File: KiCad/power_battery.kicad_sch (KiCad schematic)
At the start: 52 parts, among them IC1 BQ26221PW, J2 Conn_01x03_BATT, Q1 AO3400A, Q2 AO3400A, U2 DW01A, U3 TXS0101DBV, U4 BQ51050BRHL, U5 PAM2306AYPKE

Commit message: First Draft PCB Layout
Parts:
- renumbered C11 to C12, C12 to C13, C13 to C14, C14 to C15, C15 to C16, C16 to C17, C17 to C18, C18 to C19, C19 to C20, C20 to C21, C21 to C22, C22 to C23, C23 to C24, C24 to C25, C25 to C26, C26 to C27, C27 to C28, C28 to C29, C29 to C30, C30 to C31, C31 to C32, C32 to C33, C33 to C34
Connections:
- net AC1_C: now reaches C22.1, L1.2
- net /Red_LED_R: now reaches D2.2 (A), R16.1
- net /Blue_LED_R: now reaches D3.2 (A), R17.1
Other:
- moved on the sheet: D2, D3, R16, R17

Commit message: Implement Comments, Working on PCB Layout
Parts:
- removed C15, C16, C17: 100n, Capacitor_SMD:C_0402_1005Metric, symbol Device:C
- removed IC1: BQ26221PW, TI-BQ26221PW:SOP65P640X120-8N, symbol BQ26221PW:BQ26221PW
- removed R10, R9: 100k, Resistor_SMD:R_0402_1005Metric, symbol Device:R
- removed R11: 20m, Resistor_SMD:R_0402_1005Metric, symbol Device:R
- removed R4, R6, R8: 10k, Resistor_SMD:R_0402_1005Metric, symbol Device:R
- removed U3: TXS0101DBV, Package_TO_SOT_SMD:SOT-23-6, symbol Logic_LevelTranslator:TXS0101DBV
- added U3: MAX17262REWL_T, MAX17262REWL_T:BGA9N40P3X3_144X146X69N, symbol MAX17262REWL_T:MAX17262REWL_T
- renumbered C18 to C15, C19 to C16, C20 to C17, C21 to C18, C22 to C19, C23 to C20, C24 to C21, C25 to C22, C26 to C23, C27 to C24, C28 to C25, C29 to C26, C30 to C27, C31 to C28, C32 to C29, C33 to C30, C34 to C31, R16 to R10, R17 to R11, R7 to R4, R12 to R6, R13 to R7, R14 to R8, R15 to R9
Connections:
- net BAT_STAT_SRP is gone; now on net BATT+: C13.1
- net +1V8: no longer R5.1
- net BATT-: no longer C13.2, C14.2
- net GND: now also C13.2, C14.2, U3.B2 (ALRT), U3.C3 (GND)
- net TS_CTRL: now also R5.1
- net BATTERY_PWR renamed BATT+
- net BATT+: now also U3.A2 (BATT); no longer C28.1, C29.1, U5.1 (VIN2), U5.12 (EN2), U5.6 (EN1), U5.7 (VIN1)
- net BATT_STATUS_HDQ renamed TS_CTRL_R
- net TS_CTRL_R: now also U3.A1 (TH)
- net BAT_STAT_SRN renamed Stat_REG
- net Stat_REG: now also U3.C2 (REG)
- new net Batt_Status_SCL: U3.B1 (SCL)
- new net Batt_Status_SDA: U3.C1 (SDA)
- new net SYS_PWR: C28.1, C29.1, U3.B3 (SYS), U5.1 (VIN2), U5.12 (EN2), U5.6 (EN1), U5.7 (VIN1)
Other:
- note added: "TH - BATT if no Thermistor"
- note added: "TODO: Check Saturation Current @ 2u2"
- note removed: "GPIO unused for now"

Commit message: PCB Layout V0.1 with errors
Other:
- company: ETH Zurich: Center for Project Based Learning -> ETH Zürich: Center for Project Based Learning
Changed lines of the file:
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@@
 		(date "2026-03-09")
 		(rev "0.0.2")
-		(company "ETH Zurich: Center for Project Based Learning")
+		(company "ETH Zürich: Center for Project Based Learning")
 	)
 	(rectangle

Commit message: Fix Schematic Symbol Footprint Filter from Library for Battery
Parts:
- J2: footprint Connector_JST:JST_PH_S3B-PH-K_1x03_P2.00mm_Horizontal -> Connector_JST:JST_PH_S3B-PH-SM4-TB_1x03-1MP_P2.00mm_Horizontal
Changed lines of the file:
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@@
 			)
 		)
-		(property "Footprint" "Connector_JST:JST_PH_S3B-PH-K_1x03_P2.00mm_Horizontal"
+		(property "Footprint" "Connector_JST:JST_PH_S3B-PH-SM4-TB_1x03-1MP_P2.00mm_Horizontal"
 			(at 21.59 49.53 0)
 			(effects

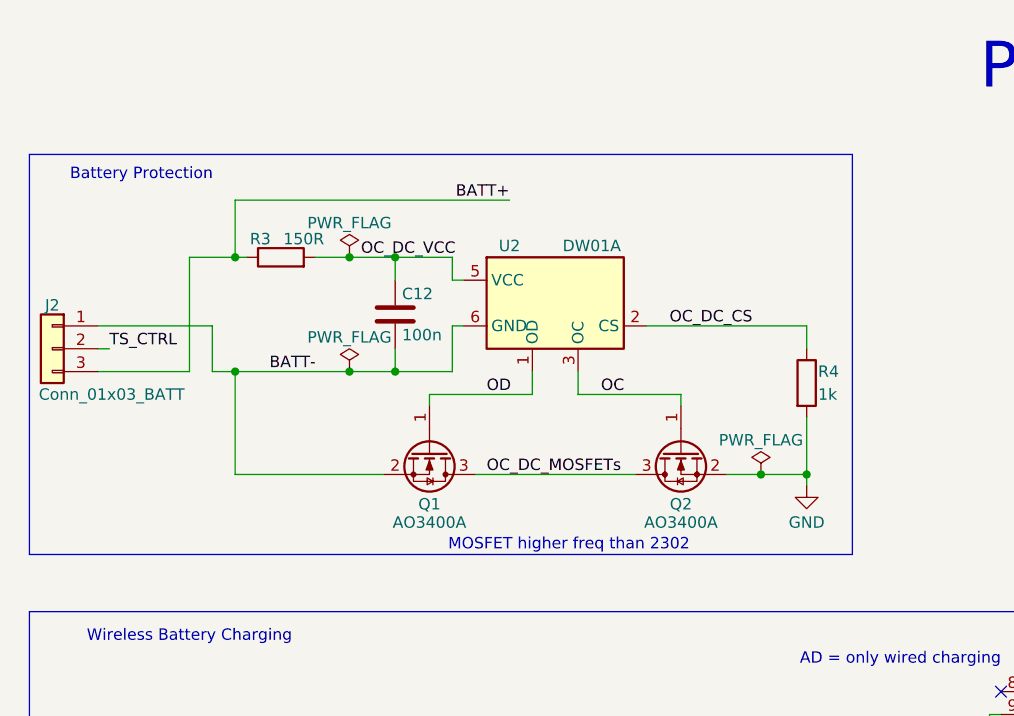
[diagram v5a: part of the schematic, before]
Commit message: Use SMT connector for Battery
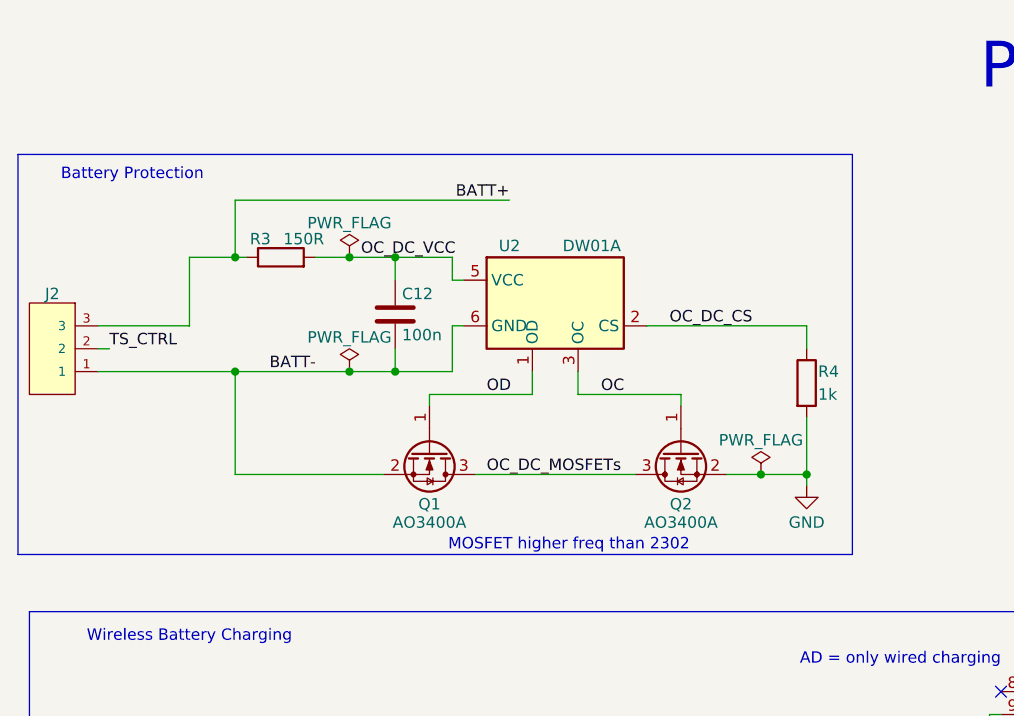
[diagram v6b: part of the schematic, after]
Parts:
- removed J2: Conn_01x03_BATT, Connector_JST:JST_PH_S3B-PH-SM4-TB_1x03-1MP_P2.00mm_Horizontal, symbol Conn-Battery:Conn_01x03_BATT
- added J2: S3B-PH-SM4-TB_LF__SN_, JST PH S3B Connector:JST_S3B-PH-SM4-TB_LF__SN_, symbol JST PH S3B Connector:S3B-PH-SM4-TB_LF__SN_
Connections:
- net BATT+: now also J2.3
- net BATT-: now also J2.1
- net TS_CTRL: now also J2.2
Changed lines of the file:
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@@
 	)
 	(rectangle
-		(start 19.05 27.94)
+		(start 17.78 27.94)
 		(end 110.49 72.39)
 		(stroke
@@
 	(text "Battery Protection"
 		(exclude_from_sim no)
-		(at 31.496 30.226 0)
+		(at 30.48 30.226 0)
 		(effects
 			(font
@@
 	(wire
 		(pts
-			(xy 26.67 52.07) (xy 36.83 52.07)
-		)
-		(stroke
-			(width 0)
-			(type default)
-		)
-	)
-	(wire
-		(pts
 			(xy 161.29 187.96) (xy 161.29 189.23)
 		)
@@
 	(wire
 		(pts
+			(xy 26.67 46.99) (xy 36.83 46.99)
+		)
+		(stroke
+			(width 0)
+			(type default)
+		)
+	)
+	(wire
+		(pts
 			(xy 54.61 39.37) (xy 59.69 39.37)
 		)
@@
 	(wire
 		(pts
-			(xy 39.37 46.99) (xy 39.37 52.07)
-		)
-		(stroke
-			(width 0)
-			(type default)
-		)
-	)
-	(wire
-		(pts
 			(xy 41.91 39.37) (xy 43.18 39.37)
 		)
@@
 	(wire
 		(pts
+			(xy 36.83 46.99) (xy 36.83 39.37)
+		)
+		(stroke
+			(width 0)
+			(type default)
+		)
+	)
+	(wire
+		(pts
 			(xy 67.31 46.99) (xy 66.04 46.99)
 		)
@@
 	(wire
 		(pts
-			(xy 36.83 39.37) (xy 36.83 52.07)
-		)
-		(stroke
-			(width 0)
-			(type default)
-		)
-	)
-	(wire
-		(pts
 			(xy 59.69 41.91) (xy 59.69 39.37)
 		)
@@
 	(wire
 		(pts
-			(xy 26.67 46.99) (xy 39.37 46.99)
-		)
-		(stroke
-			(width 0)
-			(type default)
-		)
-	)
-	(wire
-		(pts
 			(xy 168.91 140.97) (xy 177.8 140.97)
 		)
@@
 	(wire
 		(pts
-			(xy 39.37 52.07) (xy 41.91 52.07)
-		)
-		(stroke
-			(width 0)
-			(type default)
-		)
-	)
-	(wire
-		(pts
 			(xy 91.44 55.88) (xy 91.44 54.61)
 		)
@@
 	(wire
 		(pts
+			(xy 26.67 52.07) (xy 41.91 52.07)
+		)
+		(stroke
+			(width 0)
+			(type default)
+		)
+	)
+	(wire
+		(pts
 			(xy 127 171.45) (xy 142.24 171.45)
 		)
@@
 	)
 	(symbol
-		(lib_id "Conn-Battery:Conn_01x03_BATT")
-		(at 21.59 49.53 0)
-		(mirror y)
-		(unit 1)
-		(exclude_from_sim no)
-		(in_bom yes)
-		(on_board yes)
-		(dnp no)
-		(property "Reference" "J2"
-			(at 21.59 44.704 0)
-			(effects
-				(font
-					(size 1.27 1.27)
-				)
-			)
-		)
-		(property "Value" "Conn_01x03_BATT"
-			(at 28.194 54.61 0)
-			(effects
-				(font
-					(size 1.27 1.27)
-				)
-			)
-		)
-		(property "Footprint" "Connector_JST:JST_PH_S3B-PH-SM4-TB_1x03-1MP_P2.00mm_Horizontal"
-			(at 21.59 49.53 0)
-			(effects
-				(font
-					(size 1.27 1.27)
-				)
-				(hide yes)
-			)
-		)
-		(property "Datasheet" "~"
-			(at 21.59 49.53 0)
-			(effects
-				(font
-					(size 1.27 1.27)
-				)
-				(hide yes)
-			)
-		)
-		(property "Description" "Generic connector, single row, 01x03, script generated (kicad-library-utils/schlib/autogen/connector/)"
-			(at 21.59 49.53 0)
-			(effects
-				(font
-					(size 1.27 1.27)
-				)
-				(hide yes)
-			)
-		)
-		(pin "3"
-		)
-		(pin "2"
-		)
-		(pin "1"
-		)
-		(instances
-			(project ""
-				(path "/643c756f-a801-466b-9148-7370ee6a5e00/6fbfac7b-b6a0-440e-84eb-56b1f74b7943"
-					(reference "J2")
-					(unit 1)
-				)
-			)
-		)
-	)
-	(symbol
 		(lib_id "power:GND")
 		(at 139.7 142.24 0)
@@
 					(unit 1)
 				)
+			)
+		)
+	)
+	(symbol
+		(lib_id "JST PH S3B Connector:S3B-PH-SM4-TB_LF__SN_")
+		(at 21.59 49.53 180)
+		(unit 1)
+		(exclude_from_sim no)
+		(in_bom yes)
+		(on_board yes)
+		(dnp no)
+		(property "Reference" "J2"
+			(at 21.59 43.434 0)
+			(effects
+				(font
+					(size 1.27 1.27)
+				)
+			)
+		)
+		(property "Value" "S3B-PH-SM4-TB_LF__SN_"
+			(at 21.59 41.91 0)
+			(effects
+				(font
+					(size 1.27 1.27)
+				)
+				(hide yes)
+			)
+		)
+		(property "Footprint" "JST PH S3B Connector:JST_S3B-PH-SM4-TB_LF__SN_"
+			(at 21.59 49.53 0)
+			(effects
+				(font
+					(size 1.27 1.27)
+				)
+				(justify bottom)
+				(hide yes)
+			)
+		)
+		(property "Datasheet" ""
+			(at 21.59 49.53 0)
+			(effects
+				(font
+					(size 1.27 1.27)
+				)
+				(hide yes)
+			)
+		)
+		(property "Description" ""
+			(at 21.59 49.53 0)
+			(effects
+				(font
+					(size 1.27 1.27)
+				)
+				(hide yes)
+			)
+		)
+		(property "MF" "JST Sales"
+			(at 21.59 49.53 0)
+			(effects
+				(font
+					(size 1.27 1.27)
+				)
+				(justify bottom)
+				(hide yes)
+			)
+		)
+		(property "Description_1" "Connector Header Surface Mount, Right Angle 3 position 0.079 (2.00mm)"
+			(at 21.59 49.53 0)
+			(effects
+				(font
+					(size 1.27 1.27)
+				)
+				(justify bottom)
+				(hide yes)
+			)
+		)
+		(property "Package" "None"
+			(at 21.59 49.53 0)
+			(effects
+				(font
+					(size 1.27 1.27)
+				)
+				(justify bottom)
+				(hide yes)
+			)
+		)
+		(property "Price" "None"
+			(at 21.59 49.53 0)
+			(effects
+				(font
+					(size 1.27 1.27)
+				)
+				(justify bottom)
+				(hide yes)
+			)
+		)
+		(property "Check_prices" "https://www.snapeda.com/parts/S3B-PH-SM4-TB%20(LF)(SN)/JST/view-part/?ref=eda"
+			(at 21.59 49.53 0)
+			(effects
+				(font
+					(size 1.27 1.27)
+				)
+				(justify bottom)
+				(hide yes)
+			)
+		)
+		(property "STANDARD" "MANUFACTURER RECOMMENDATIONS"
+			(at 21.59 49.53 0)
+			(effects
+				(font
+					(size 1.27 1.27)
+				)
+				(justify bottom)
+				(hide yes)
+			)
+		)
+		(property "PARTREV" "NA"
+			(at 21.59 49.53 0)
+			(effects
+				(font
+					(size 1.27 1.27)
+				)
+				(justify bottom)
+				(hide yes)
+			)
+		)
+		(property "SnapEDA_Link" "https://www.snapeda.com/parts/S3B-PH-SM4-TB%20(LF)(SN)/JST/view-part/?ref=snap"
+			(at 21.59 49.53 0)
+			(effects
+				(font
+					(size 1.27 1.27)
+				)
+				(justify bottom)
+				(hide yes)
+			)
+		)
+		(property "MP" "S3B-PH-SM4-TB (LF)(SN)"
+			(at 21.59 49.53 0)
+			(effects
+				(font
+					(size 1.27 1.27)
+				)
+				(justify bottom)
+				(hide yes)
+			)
+		)
+		(property "Availability" "In Stock"
+			(at 21.59 49.53 0)
+			(effects
+				(font
+					(size 1.27 1.27)
+				)
+				(justify bottom)
+				(hide yes)
+			)
+		)
+		(property "MANUFACTURER" "JST"
+			(at 21.59 49.53 0)
+			(effects
+				(font
+					(size 1.27 1.27)
+				)
+				(justify bottom)
+				(hide yes)
+			)
+		)
+		(pin "1"
+		)
+		(pin "3"
+		)
+		(pin "2"
+		)
+		(instances
+			(project ""
+				(path "/643c756f-a801-466b-9148-7370ee6a5e00/6fbfac7b-b6a0-440e-84eb-56b1f74b7943"
+					(reference "J2")
+					(unit 1)
+				)

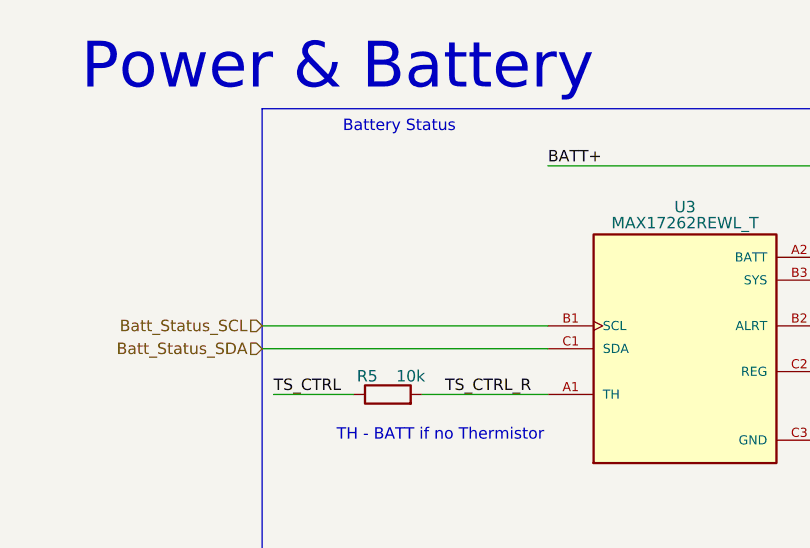
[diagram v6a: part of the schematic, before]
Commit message: V2 beginning with buttons, resistor, ...
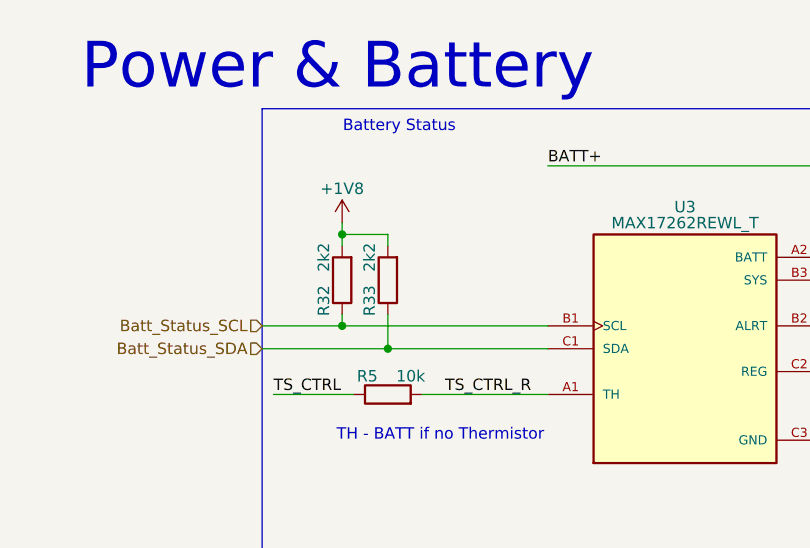
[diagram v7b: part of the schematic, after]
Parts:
- added R32, R33: 2k2, Resistor_SMD:R_0402_1005Metric, symbol Device:R
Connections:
- net +1V8: now also R32.2, R33.2
- net Batt_Status_SCL: now also R32.1
- net Batt_Status_SDA: now also R33.1
